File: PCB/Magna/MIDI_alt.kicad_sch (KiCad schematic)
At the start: 32 parts, among them J1001 DIN-5_180degree, J1002 DIN-5_180degree, J1003 DIN-5_180degree, U1001 74LVC2G14, U1002 74LVC2G14, U1003 74HC08D, U1004 TLP2361

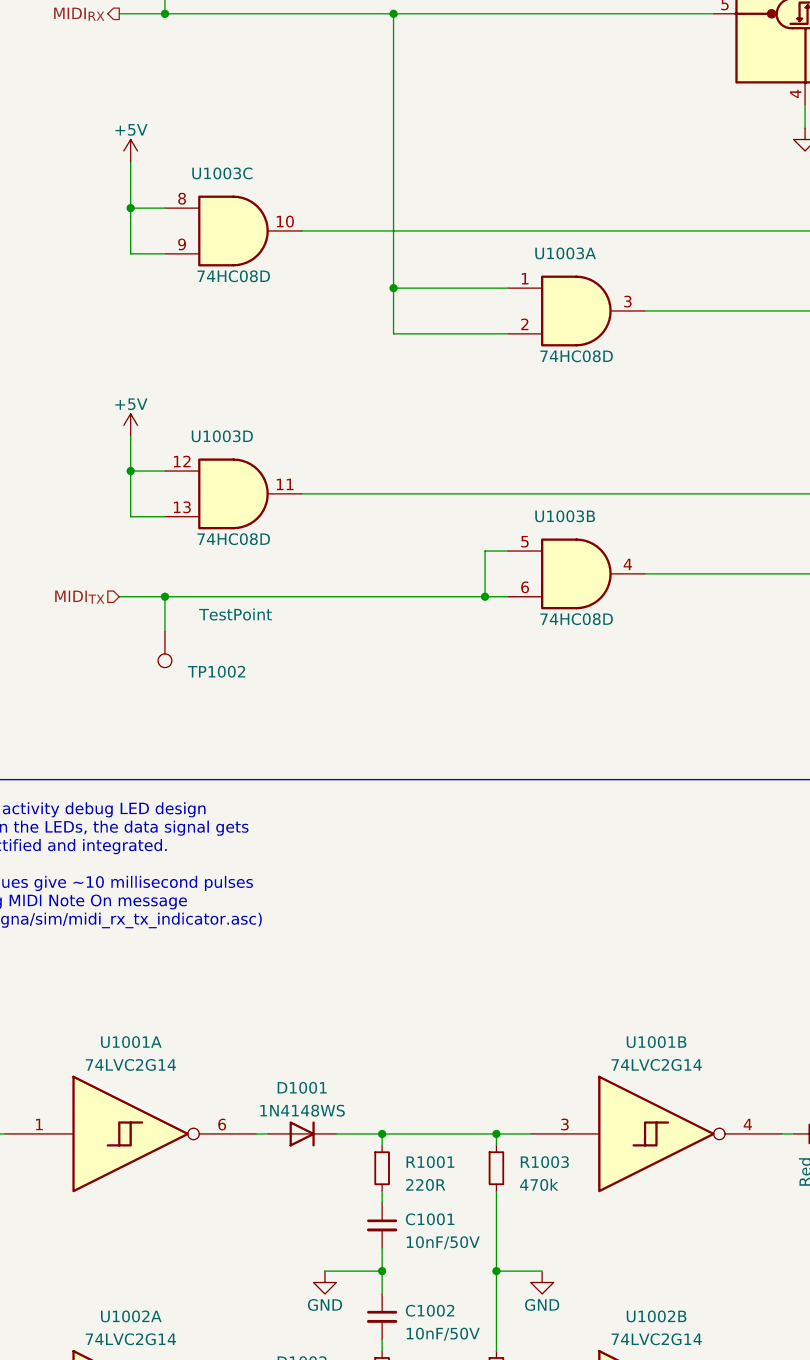
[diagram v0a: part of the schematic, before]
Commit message: Start of layout for Mainboard PCB
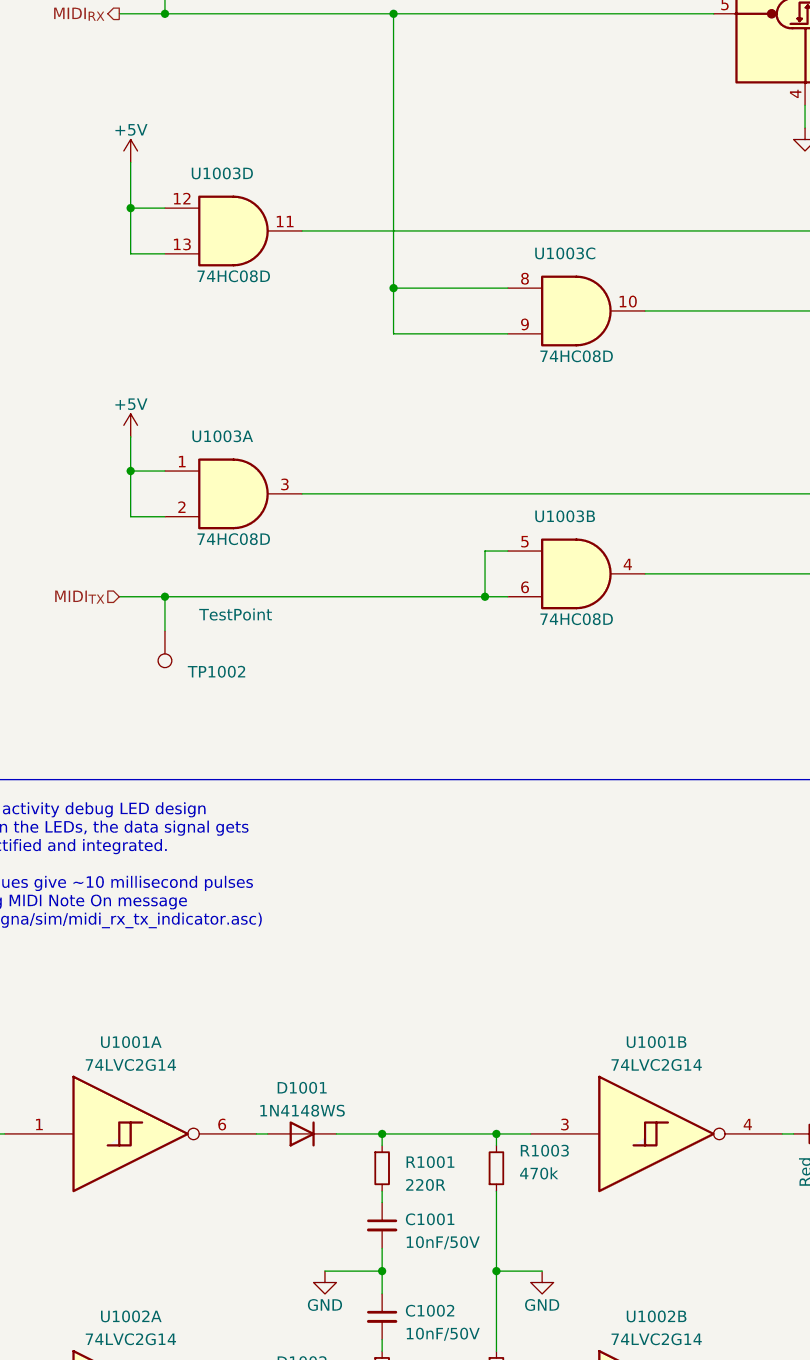
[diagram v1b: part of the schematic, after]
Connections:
- net +5V: now also U1003.1, U1003.2; no longer U1003.8, U1003.9
- net GND: now also R1003.1; no longer R1003.2
- net MIDI_{RX}: now also U1003.8, U1003.9; no longer U1003.1, U1003.2
- net at R1010.1: now also U1003.3; no longer U1003.11
- net at D1001.1 (K), R1001.1, U1001.3: now also R1003.2; no longer R1003.1
- net at R1008.1: now also U1003.11; no longer U1003.10
- net at R1009.1: now also U1003.10; no longer U1003.3
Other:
- moved on the sheet: U1003A, U1003C, U1003D
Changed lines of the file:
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@@
     )
   )
-  (symbol (lib_id "4xxx:4081") (at 52.07 85.09 0) (unit 4)
-    (in_bom yes) (on_board yes) (dnp no)
-    (property "Reference" "U1003" (at 50.8 78.74 0)
-      (effects (font (size 1.27 1.27)))
-    )
-    (property "Value" "74HC08D" (at 52.07 90.17 0)
-      (effects (font (size 1.27 1.27)))
-    )
-    (property "Footprint" "Package_SO:SOIC-14_3.9x8.7mm_P1.27mm" (at 52.07 85.09 0)
-      (effects (font (size 1.27 1.27)) hide)
-    )
-    (property "Datasheet" "http://www.intersil.com/content/dam/Intersil/documents/cd40/cd4073bms-81bms-82bms.pdf" (at 52.07 85.09 0)
-      (effects (font (size 1.27 1.27)) hide)
-    )
-    (property "LCSC" "C5593" (at 52.07 85.09 0)
+  (symbol (lib_id "4xxx:4081") (at 52.07 55.88 0) (unit 4)
+    (in_bom yes) (on_board yes) (dnp no)
+    (property "Reference" "U1003" (at 50.8 49.53 0)
+      (effects (font (size 1.27 1.27)))
+    )
+    (property "Value" "74HC08D" (at 52.07 60.96 0)
+      (effects (font (size 1.27 1.27)))
+    )
+    (property "Footprint" "Package_SO:SOIC-14_3.9x8.7mm_P1.27mm" (at 52.07 55.88 0)
+      (effects (font (size 1.27 1.27)) hide)
+    )
+    (property "Datasheet" "http://www.intersil.com/content/dam/Intersil/documents/cd40/cd4073bms-81bms-82bms.pdf" (at 52.07 55.88 0)
+      (effects (font (size 1.27 1.27)) hide)
+    )
+    (property "LCSC" "C5593" (at 52.07 55.88 0)
       (effects (font (size 1.27 1.27)) hide)
     )
@@
     )
   )
-  (symbol (lib_id "4xxx:4081") (at 90.17 64.77 0) (unit 1)
-    (in_bom yes) (on_board yes) (dnp no)
-    (property "Reference" "U1003" (at 88.9 58.42 0)
-      (effects (font (size 1.27 1.27)))
-    )
-    (property "Value" "74HC08D" (at 90.17 69.85 0)
-      (effects (font (size 1.27 1.27)))
-    )
-    (property "Footprint" "Package_SO:SOIC-14_3.9x8.7mm_P1.27mm" (at 90.17 64.77 0)
-      (effects (font (size 1.27 1.27)) hide)
-    )
-    (property "Datasheet" "http://www.intersil.com/content/dam/Intersil/documents/cd40/cd4073bms-81bms-82bms.pdf" (at 90.17 64.77 0)
-      (effects (font (size 1.27 1.27)) hide)
-    )
-    (property "LCSC" "C5593" (at 90.17 64.77 0)
+  (symbol (lib_id "4xxx:4081") (at 52.07 85.09 0) (unit 1)
+    (in_bom yes) (on_board yes) (dnp no)
+    (property "Reference" "U1003" (at 50.8 78.74 0)
+      (effects (font (size 1.27 1.27)))
+    )
+    (property "Value" "74HC08D" (at 52.07 90.17 0)
+      (effects (font (size 1.27 1.27)))
+    )
+    (property "Footprint" "Package_SO:SOIC-14_3.9x8.7mm_P1.27mm" (at 52.07 85.09 0)
+      (effects (font (size 1.27 1.27)) hide)
+    )
+    (property "Datasheet" "http://www.intersil.com/content/dam/Intersil/documents/cd40/cd4073bms-81bms-82bms.pdf" (at 52.07 85.09 0)
+      (effects (font (size 1.27 1.27)) hide)
+    )
+    (property "LCSC" "C5593" (at 52.07 85.09 0)
       (effects (font (size 1.27 1.27)) hide)
     )
@@
     )
   )
-  (symbol (lib_id "Device:R_Small") (at 81.28 160.02 0) (unit 1)
-    (in_bom yes) (on_board yes) (dnp no) (fields_autoplaced)
-    (property "Reference" "R1003" (at 83.82 159.385 0)
-      (effects (font (size 1.27 1.27)) (justify left))
-    )
-    (property "Value" "470k" (at 83.82 161.925 0)
+  (symbol (lib_id "Device:R_Small") (at 81.28 160.02 0) (mirror x) (unit 1)
+    (in_bom yes) (on_board yes) (dnp no)
+    (property "Reference" "R1003" (at 83.82 158.115 0)
+      (effects (font (size 1.27 1.27)) (justify left))
+    )
+    (property "Value" "470k" (at 83.82 160.655 0)
       (effects (font (size 1.27 1.27)) (justify left))
     )
@@
     )
   )
-  (symbol (lib_id "4xxx:4081") (at 52.07 55.88 0) (unit 3)
-    (in_bom yes) (on_board yes) (dnp no)
-    (property "Reference" "U1003" (at 50.8 49.53 0)
-      (effects (font (size 1.27 1.27)))
-    )
-    (property "Value" "74HC08D" (at 52.07 60.96 0)
-      (effects (font (size 1.27 1.27)))
-    )
-    (property "Footprint" "Package_SO:SOIC-14_3.9x8.7mm_P1.27mm" (at 52.07 55.88 0)
-      (effects (font (size 1.27 1.27)) hide)
-    )
-    (property "Datasheet" "http://www.intersil.com/content/dam/Intersil/documents/cd40/cd4073bms-81bms-82bms.pdf" (at 52.07 55.88 0)
-      (effects (font (size 1.27 1.27)) hide)
-    )
-    (property "LCSC" "C5593" (at 52.07 55.88 0)
-      (effects (font (size 1.27 1.27)) hide)
-    )
+  (symbol (lib_id "4xxx:4081") (at 90.17 64.77 0) (unit 3)
+    (in_bom yes) (on_board yes) (dnp no)
+    (property "Reference" "U1003" (at 88.9 58.42 0)
+      (effects (font (size 1.27 1.27)))
+    )
+    (property "Value" "74HC08D" (at 90.17 69.85 0)
+      (effects (font (size 1.27 1.27)))
+    )
+    (property "Footprint" "Package_SO:SOIC-14_3.9x8.7mm_P1.27mm" (at 90.17 64.77 0)
+      (effects (font (size 1.27 1.27)) hide)
+    )
+    (property "Datasheet" "http://www.intersil.com/content/dam/Intersil/documents/cd40/cd4073bms-81bms-82bms.pdf" (at 90.17 64.77 0)
+      (effects (font (size 1.27 1.27)) hide)
+    )
+    (property "LCSC" "C5593" (at 90.17 64.77 0)
+      (effects (font (size 1.27 1.27)) hide)
+    )

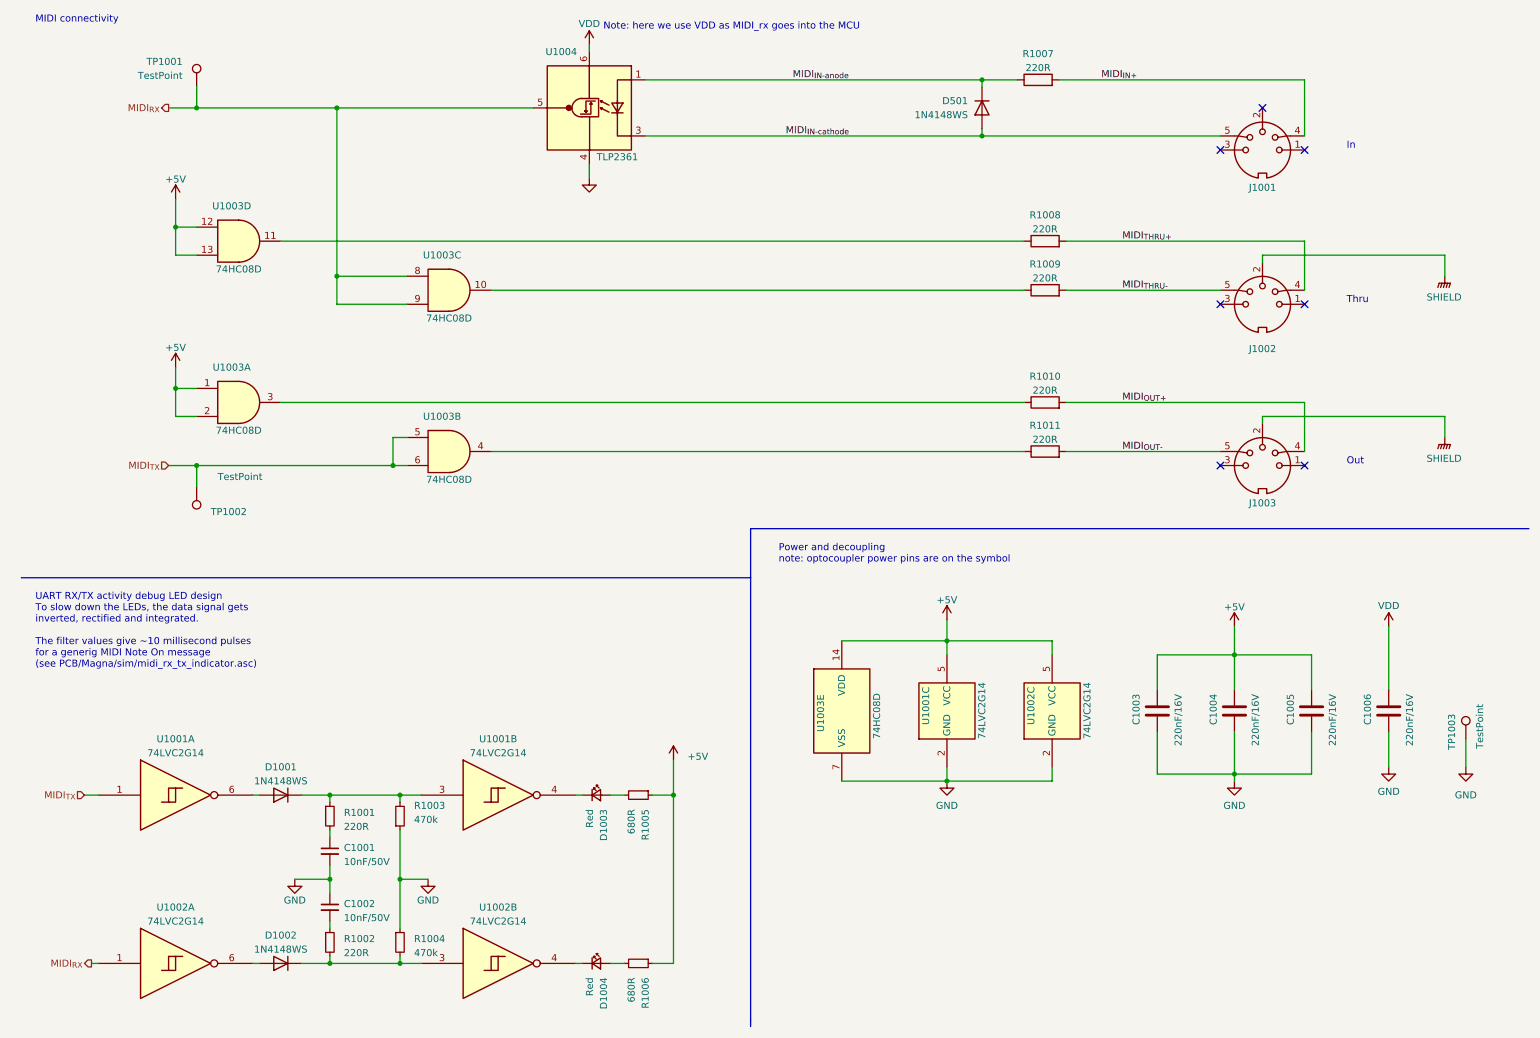
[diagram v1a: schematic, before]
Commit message: Add more traces to the PCB
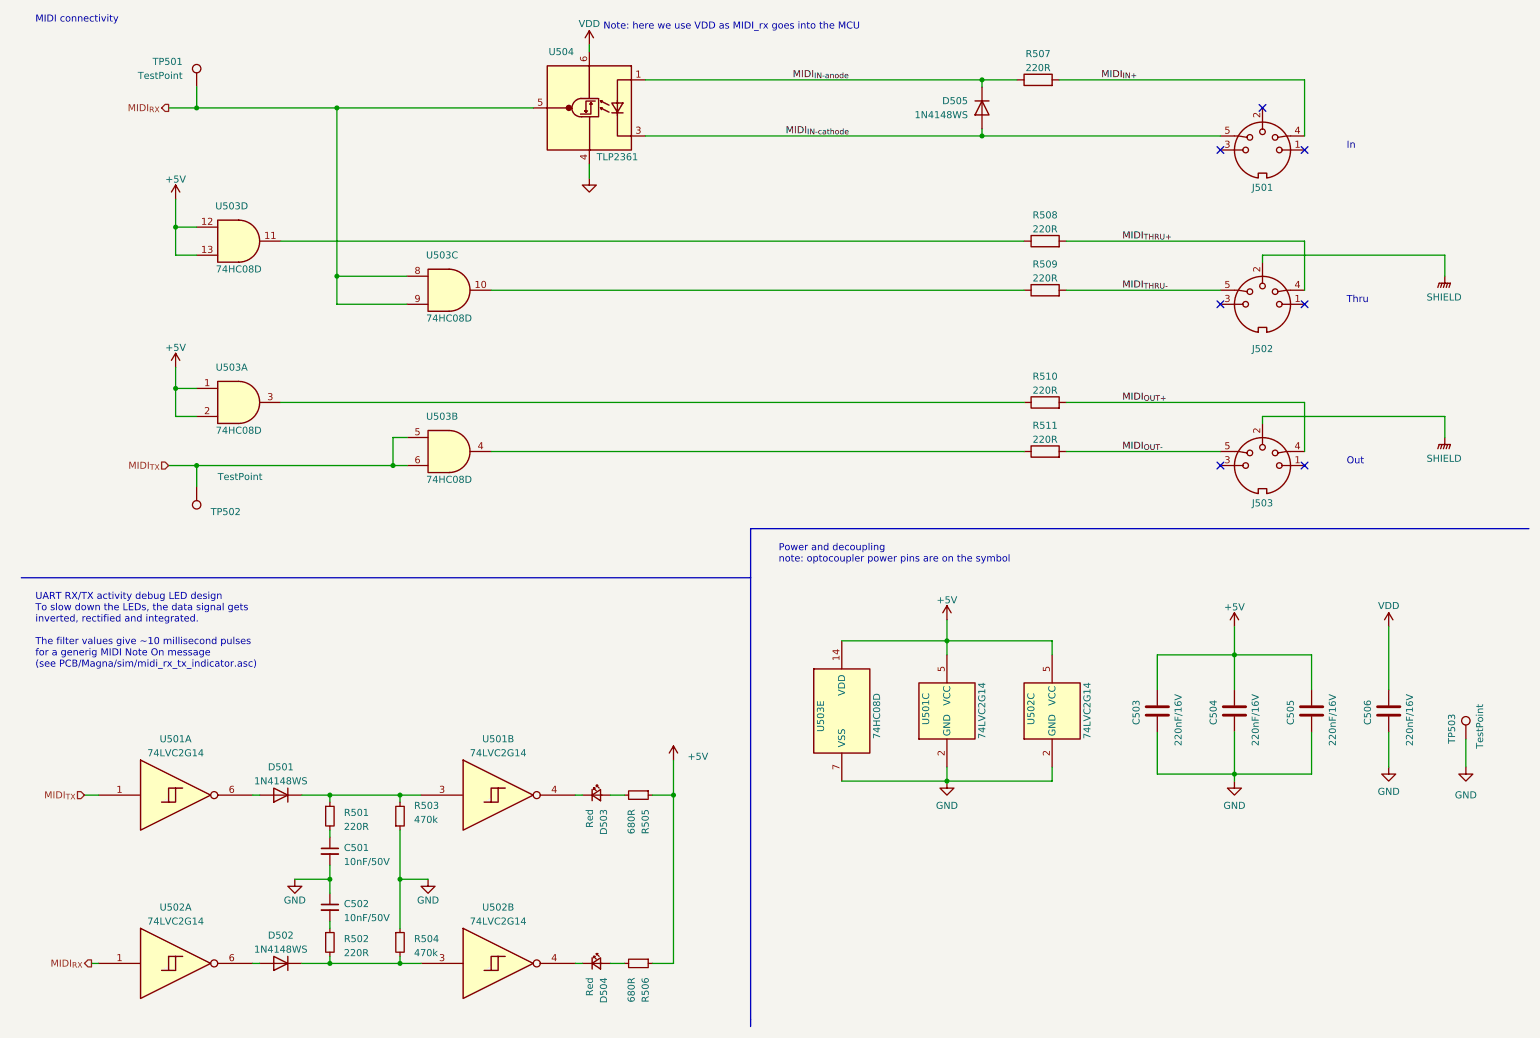
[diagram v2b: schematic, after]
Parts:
- renumbered C1001 to C501, C1002 to C502, C1003 to C503, C1004 to C504, C1005 to C505, C1006 to C506, D1001 to D501, D1002 to D502, D1003 to D503, D1004 to D504, D501 to D505, J1001 to J501, J1002 to J502, J1003 to J503, R1001 to R501, R1002 to R502, R1003 to R503, R1004 to R504, R1005 to R505, R1006 to R506, R1007 to R507, R1008 to R508, R1009 to R509, R1010 to R510, R1011 to R511, TP1001 to TP501, TP1002 to TP502, TP1003 to TP503, U1001 to U501, U1002 to U502, U1003 to U503, U1004 to U504
